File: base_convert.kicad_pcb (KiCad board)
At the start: 2 copper layers, 93.3 x 100 mm, 96 parts, among them J1 ISP, J3 Vin, Q1 Q_PMOS_GSD, Q10 Q_PNP_BEC, Q11 Q_PNP_BEC, Q12 Q_PNP_BEC, Q13 Q_PNP_BEC, Q14 Q_PNP_BEC, Q15 Q_PNP_BEC, Q16 Q_PNP_BEC, Q17 Q_PNP_BEC, Q18 Q_PNP_BEC, Q19 Q_PNP_BEC, Q2 Q_PNP_BEC, Q20 Q_NPN_BEC, Q21 Q_NPN_BEC, Q22 Q_NPN_BEC, Q23 Q_NPN_BEC, Q24 Q_NPN_BEC, Q25 Q_NPN_BEC, Q26 Q_NPN_BEC, Q27 Q_NPN_BEC, Q3 Q_PNP_BEC, Q4 Q_PNP_BEC, Q5 Q_PNP_BEC, Q6 Q_NPN_BEC, Q7 Q_NPN_BEC, Q8 Q_NPN_BEC, Q9 Q_NPN_BEC, SW1 SELECT, SW10 1, SW11 4, SW12 7, SW13 A, SW14 CLEAR, SW15 B, SW16 C, SW17 D, SW18 E, SW2 3, SW3 6, SW4 9, SW5 F, SW6 2, SW7 5, SW8 8, SW9 0, U1 MIC5317-3.3YM5-TR, U2 MSP430FR2033IPMR

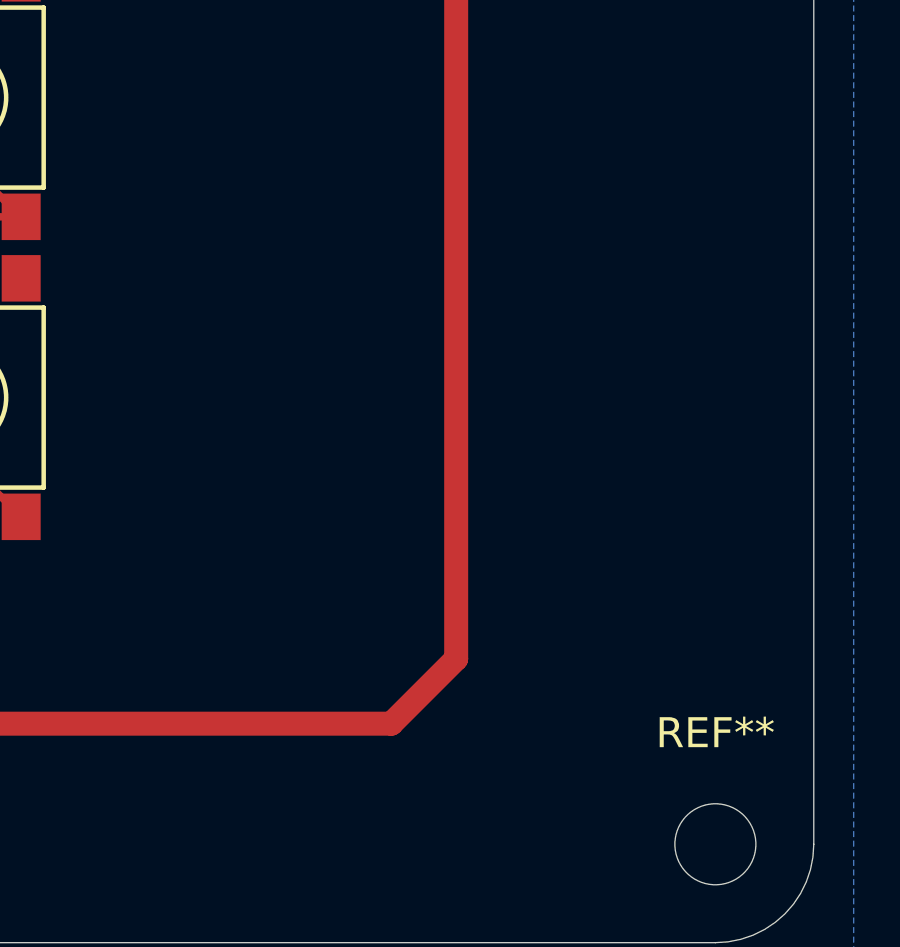
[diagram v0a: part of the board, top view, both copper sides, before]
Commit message: add logo
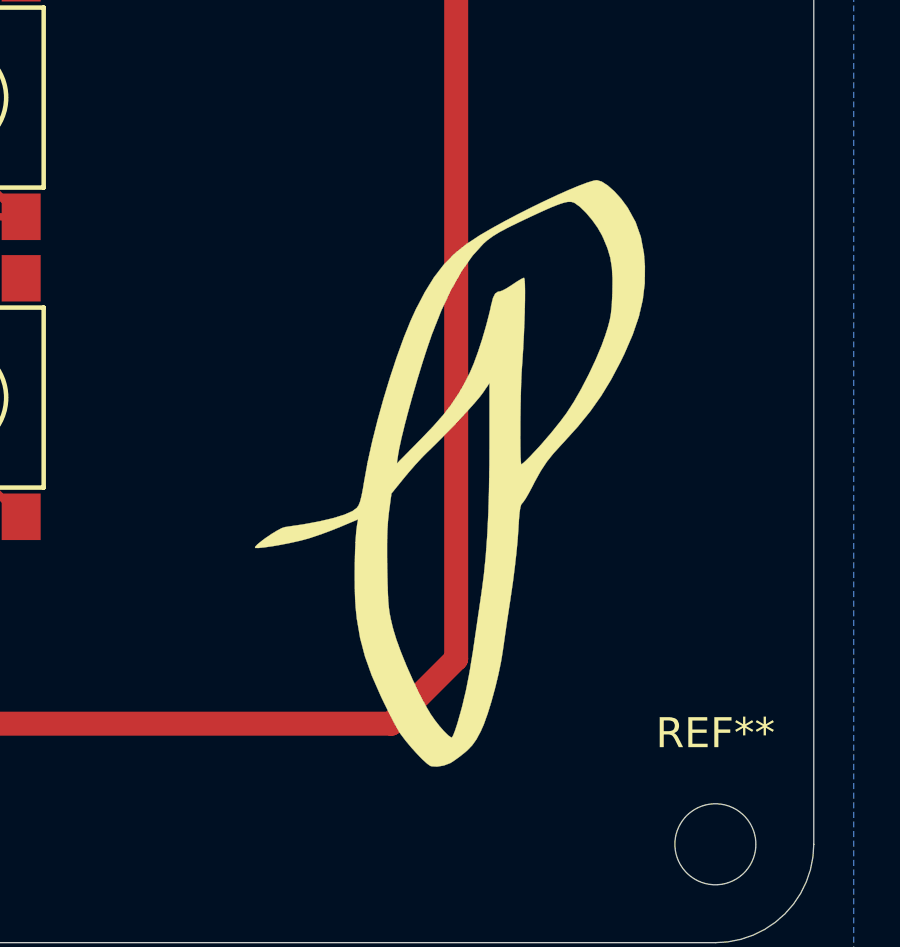
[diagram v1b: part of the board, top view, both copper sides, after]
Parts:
- added G***: LOGO, PL_logo:logo_height_20mm, F.Cu at (134.5, 134.4)
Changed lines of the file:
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@@
 (kicad_pcb (version 4) (host pcbnew 4.0.7)
   (general
-    (links 237)
+    (links 0)
     (no_connects 0)
     (area 52 48.605 148.000001 151.000001)
@@
     (tracks 1310)
     (zones 0)
-    (modules 96)
+    (modules 97)
     (nets 112)
   )
@@
     (34 B.Paste user hide)
     (35 F.Paste user hide)
-    (36 B.SilkS user hide)
-    (37 F.SilkS user hide)
+    (36 B.SilkS user)
+    (37 F.SilkS user)
     (38 B.Mask user hide)
     (39 F.Mask user hide)
@@
     (pad 1 np_thru_hole circle (at 0 0) (size 2.7 2.7) (drill 2.7) (layers *.Cu *.Mask))
   )
+  (module PL_logo:logo_height_20mm (layer F.Cu)
+    (at 134.49 134.4)
+    (fp_text reference G*** (at 0 0) (layer F.SilkS) hide
+      (effects (font (thickness 0.3)))
+    )
+    (fp_text value LOGO (at 0.75 0) (layer F.SilkS) hide
+      (effects (font (thickness 0.3)))
+    )
+    (fp_poly (pts (xy 5.110447 -9.770652) (xy 5.312269 -9.640666) (xy 5.534322 -9.443902) (xy 5.758485 -9.196577)
+      (xy 5.96664 -8.914909) (xy 5.98231 -8.890989) (xy 6.239473 -8.422228) (xy 6.416068 -7.923876)
+      (xy 6.519396 -7.371012) (xy 6.551677 -6.947643) (xy 6.545956 -6.381247) (xy 6.479614 -5.82589)
+      (xy 6.347459 -5.261244) (xy 6.144301 -4.666981) (xy 5.864947 -4.022772) (xy 5.737802 -3.760784)
+      (xy 5.422669 -3.165189) (xy 5.093822 -2.62529) (xy 4.731023 -2.1127) (xy 4.314034 -1.599035)
+      (xy 3.822617 -1.055909) (xy 3.768597 -0.998877) (xy 3.49642 -0.699627) (xy 3.277407 -0.423662)
+      (xy 3.085305 -0.133221) (xy 2.89386 0.209456) (xy 2.796977 0.398632) (xy 2.681419 0.617345)
+      (xy 2.574296 0.800024) (xy 2.491792 0.919921) (xy 2.464519 0.948195) (xy 2.427285 0.998544)
+      (xy 2.397557 1.099049) (xy 2.373053 1.26548) (xy 2.351492 1.513606) (xy 2.330594 1.859196)
+      (xy 2.329359 1.882471) (xy 2.305361 2.215766) (xy 2.265794 2.627183) (xy 2.214545 3.082356)
+      (xy 2.155502 3.54692) (xy 2.09255 3.986509) (xy 2.088075 4.015605) (xy 2.026235 4.419717)
+      (xy 1.966076 4.820335) (xy 1.911374 5.191749) (xy 1.865906 5.508247) (xy 1.833449 5.744119)
+      (xy 1.827804 5.787522) (xy 1.764501 6.187507) (xy 1.67347 6.63336) (xy 1.562106 7.097654)
+      (xy 1.437803 7.552962) (xy 1.307955 7.971858) (xy 1.179956 8.326913) (xy 1.084112 8.546046)
+      (xy 0.937302 8.819355) (xy 0.794637 9.022883) (xy 0.62642 9.195872) (xy 0.530816 9.277194)
+      (xy 0.347846 9.420104) (xy 0.178277 9.542154) (xy 0.059975 9.616254) (xy -0.151123 9.695147)
+      (xy -0.374715 9.732273) (xy -0.561955 9.720841) (xy -0.600957 9.708124) (xy -0.708554 9.634028)
+      (xy -0.865156 9.490665) (xy -1.050824 9.299752) (xy -1.245621 9.08301) (xy -1.429608 8.862157)
+      (xy -1.582846 8.658913) (xy -1.634056 8.582753) (xy -1.724533 8.427502) (xy -1.849762 8.193559)
+      (xy -1.996847 7.905971) (xy -2.152891 7.589783) (xy -2.253941 7.378834) (xy -2.553552 6.696073)
+      (xy -2.780259 6.060909) (xy -2.943151 5.441507) (xy -3.051318 4.806034) (xy -3.089538 4.452134)
+      (xy -3.108839 4.147395) (xy -3.120082 3.777455) (xy -3.123672 3.36871) (xy -3.120014 2.947556)
+      (xy -3.109511 2.540389) (xy -3.097113 2.272005) (xy -2.042954 2.272005) (xy -2.04283 2.749466)
+      (xy -2.036487 3.167865) (xy -2.027131 3.598264) (xy -2.016838 3.936345) (xy -2.003406 4.203938)
+      (xy -1.984633 4.422876) (xy -1.95832 4.61499) (xy -1.922265 4.802112) (xy -1.874267 5.006072)
+      (xy -1.835999 5.156553) (xy -1.730964 5.501704) (xy -1.579822 5.91545) (xy -1.39543 6.368634)
+      (xy -1.190641 6.832099) (xy -0.978312 7.276687) (xy -0.771297 7.673242) (xy -0.592437 7.97709)
+      (xy -0.449521 8.183624) (xy -0.292517 8.38383) (xy -0.138809 8.558643) (xy -0.005783 8.689)
+      (xy 0.089178 8.755836) (xy 0.119772 8.758103) (xy 0.157698 8.692735) (xy 0.21601 8.544905)
+      (xy 0.284254 8.342064) (xy 0.309684 8.259381) (xy 0.460399 7.720907) (xy 0.589537 7.175597)
+      (xy 0.704348 6.589349) (xy 0.81208 5.928063) (xy 0.827759 5.822461) (xy 0.888257 5.410055)
+      (xy 0.957618 4.936465) (xy 1.028263 4.453473) (xy 1.092615 4.012863) (xy 1.107636 3.909887)
+      (xy 1.183113 3.33022) (xy 1.244733 2.715647) (xy 1.2932 2.052558) (xy 1.329222 1.327348)
+      (xy 1.353506 0.526409) (xy 1.366756 -0.363868) (xy 1.369888 -1.142652) (xy 1.369888 -3.052185)
+      (xy 1.159111 -2.739014) (xy 1.043555 -2.587637) (xy 0.860782 -2.372867) (xy 0.625694 -2.110611)
+      (xy 0.35319 -1.816778) (xy 0.058172 -1.507274) (xy -0.244461 -1.198009) (xy -0.539807 -0.90489)
+      (xy -0.732942 -0.719056) (xy -0.897814 -0.551888) (xy -1.103188 -0.327672) (xy -1.31941 -0.079417)
+      (xy -1.467688 0.09879) (xy -1.897581 0.627835) (xy -1.980084 1.241445) (xy -2.01215 1.537418)
+      (xy -2.032917 1.874463) (xy -2.042954 2.272005) (xy -3.097113 2.272005) (xy -3.092567 2.173606)
+      (xy -3.069586 1.873602) (xy -3.047424 1.701141) (xy -3.011222 1.490147) (xy -3.603252 1.740546)
+      (xy -3.913187 1.864764) (xy -4.253148 1.990126) (xy -4.570058 2.097455) (xy -4.708989 2.140026)
+      (xy -4.961993 2.20636) (xy -5.256046 2.2724) (xy -5.565525 2.333672) (xy -5.864807 2.385699)
+      (xy -6.128268 2.424005) (xy -6.330287 2.444114) (xy -6.440733 2.44253) (xy -6.443846 2.406481)
+      (xy -6.369386 2.326813) (xy -6.238015 2.218057) (xy -6.070397 2.094748) (xy -5.887193 1.971418)
+      (xy -5.709067 1.862599) (xy -5.55668 1.782823) (xy -5.45142 1.746718) (xy -4.82984 1.654577)
+      (xy -4.286919 1.553549) (xy -3.829866 1.445555) (xy -3.465892 1.332515) (xy -3.202205 1.21635)
+      (xy -3.053996 1.107951) (xy -2.995972 1.025898) (xy -2.945791 0.904301) (xy -2.898135 0.723744)
+      (xy -2.847687 0.464808) (xy -2.801264 0.185151) (xy -2.699695 -0.371012) (xy -1.71808 -0.371012)
+      (xy -0.912748 -1.18778) (xy -0.506321 -1.612275) (xy -0.173333 -1.990833) (xy 0.103453 -2.346866)
+      (xy 0.341276 -2.703785) (xy 0.557374 -3.085004) (xy 0.713275 -3.39618) (xy 0.845662 -3.705274)
+      (xy 0.988099 -4.093966) (xy 1.130249 -4.529533) (xy 1.261771 -4.97925) (xy 1.372328 -5.410396)
+      (xy 1.424366 -5.646894) (xy 1.486632 -5.890114) (xy 1.559501 -6.035739) (xy 1.653241 -6.10033)
+      (xy 1.709886 -6.107416) (xy 1.803792 -6.138716) (xy 1.956032 -6.220771) (xy 2.133521 -6.335731)
+      (xy 2.304954 -6.449923) (xy 2.443933 -6.5318) (xy 2.520975 -6.564026) (xy 2.521823 -6.564045)
+      (xy 2.539593 -6.509571) (xy 2.550554 -6.356119) (xy 2.555057 -6.118642) (xy 2.553451 -5.812094)
+      (xy 2.546088 -5.45143) (xy 2.533316 -5.051604) (xy 2.515486 -4.627569) (xy 2.492949 -4.19428)
+      (xy 2.466053 -3.766691) (xy 2.451665 -3.567416) (xy 2.437554 -3.331244) (xy 2.425449 -3.03294)
+      (xy 2.41546 -2.689467) (xy 2.4077 -2.317787) (xy 2.402282 -1.934861) (xy 2.399317 -1.557652)
+      (xy 2.398917 -1.20312) (xy 2.401195 -0.888229) (xy 2.406263 -0.629939) (xy 2.414232 -0.445213)
+      (xy 2.425215 -0.351011) (xy 2.430349 -0.342472) (xy 2.484805 -0.38002) (xy 2.592384 -0.477421)
+      (xy 2.701472 -0.585057) (xy 3.055369 -0.96369) (xy 3.416394 -1.381698) (xy 3.749052 -1.796963)
+      (xy 3.938592 -2.05297) (xy 4.174713 -2.416169) (xy 4.426061 -2.855489) (xy 4.675934 -3.337451)
+      (xy 4.907627 -3.828575) (xy 5.104436 -4.295382) (xy 5.228975 -4.63929) (xy 5.316414 -4.916881)
+      (xy 5.37705 -5.143794) (xy 5.416914 -5.356555) (xy 5.442038 -5.591687) (xy 5.458451 -5.885713)
+      (xy 5.465453 -6.071296) (xy 5.471388 -6.527629) (xy 5.450072 -6.904527) (xy 5.395514 -7.234718)
+      (xy 5.301721 -7.550929) (xy 5.162699 -7.885885) (xy 5.114386 -7.988458) (xy 4.972109 -8.238033)
+      (xy 4.788131 -8.495248) (xy 4.584747 -8.734412) (xy 4.384252 -8.929835) (xy 4.208941 -9.055824)
+      (xy 4.173444 -9.07273) (xy 4.09124 -9.094614) (xy 3.989089 -9.094277) (xy 3.855089 -9.067416)
+      (xy 3.677339 -9.00973) (xy 3.443938 -8.91692) (xy 3.142982 -8.784682) (xy 2.762572 -8.608718)
+      (xy 2.356567 -8.416162) (xy 1.985432 -8.234109) (xy 1.699223 -8.081259) (xy 1.476723 -7.944798)
+      (xy 1.296718 -7.811912) (xy 1.167101 -7.697722) (xy 0.803408 -7.29618) (xy 0.446701 -6.788609)
+      (xy 0.101554 -6.183108) (xy -0.227457 -5.487781) (xy -0.535755 -4.71073) (xy -0.563786 -4.632993)
+      (xy -0.715261 -4.192448) (xy -0.873007 -3.703403) (xy -1.031467 -3.185769) (xy -1.185084 -2.659456)
+      (xy -1.328301 -2.144377) (xy -1.455563 -1.66044) (xy -1.561311 -1.227556) (xy -1.639989 -0.865638)
+      (xy -1.681547 -0.627866) (xy -1.71808 -0.371012) (xy -2.699695 -0.371012) (xy -2.689515 -0.426754)
+      (xy -2.541231 -1.098048) (xy -2.363085 -1.806575) (xy -2.161753 -2.53018) (xy -1.943909 -3.246706)
+      (xy -1.716226 -3.933999) (xy -1.485378 -4.569901) (xy -1.258041 -5.132258) (xy -1.086226 -5.50809)
+      (xy -0.781415 -6.091052) (xy -0.478181 -6.580316) (xy -0.160039 -6.994905) (xy 0.189496 -7.35384)
+      (xy 0.58691 -7.676144) (xy 1.048687 -7.980837) (xy 1.065546 -7.991012) (xy 1.442899 -8.210713)
+      (xy 1.858246 -8.439635) (xy 2.297431 -8.671115) (xy 2.746294 -8.89849) (xy 3.19068 -9.115098)
+      (xy 3.61643 -9.314276) (xy 4.009387 -9.489361) (xy 4.355394 -9.633692) (xy 4.640293 -9.740605)
+      (xy 4.849927 -9.803437) (xy 4.946973 -9.817643) (xy 5.110447 -9.770652)) (layer F.SilkS) (width 0.01))
+  )
   (gr_line (start 141.67 55) (end 58.33 55) (layer Dwgs.User) (width 0.01))

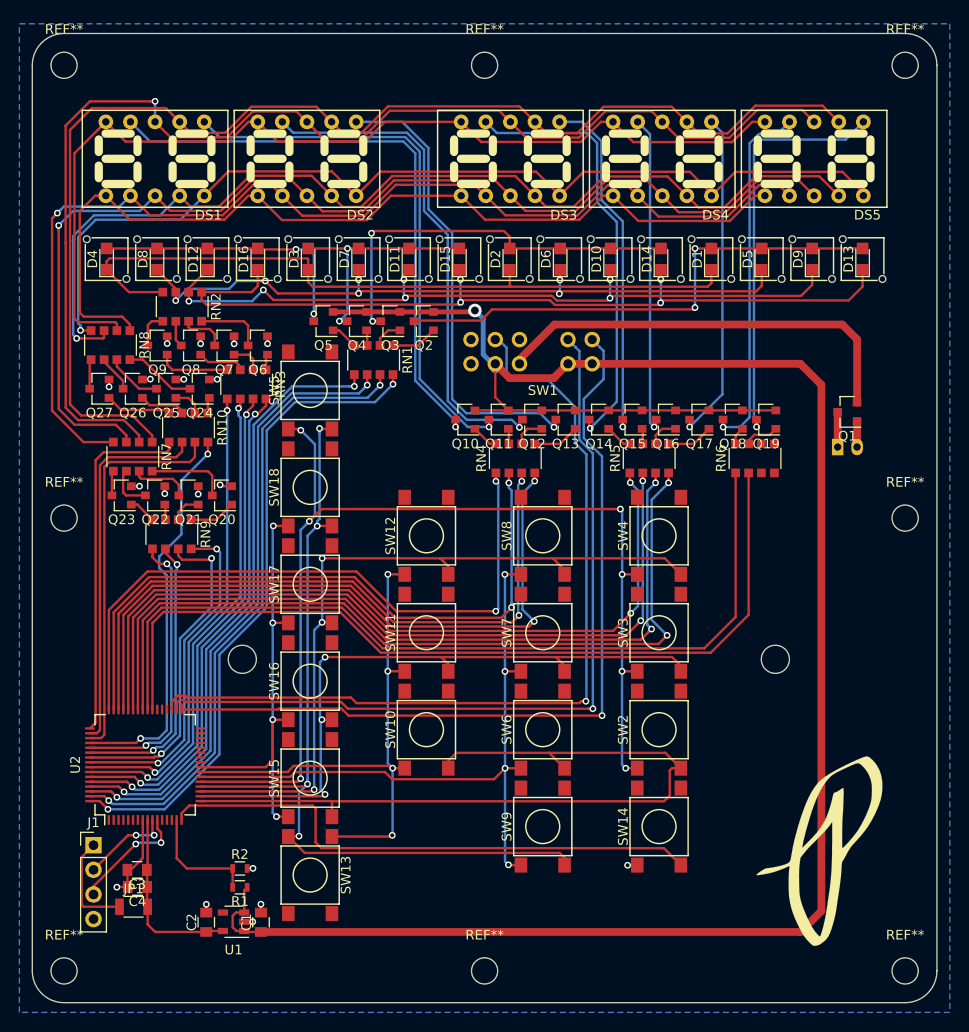
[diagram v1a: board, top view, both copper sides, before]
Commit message: clean up silkscreen, as sn label
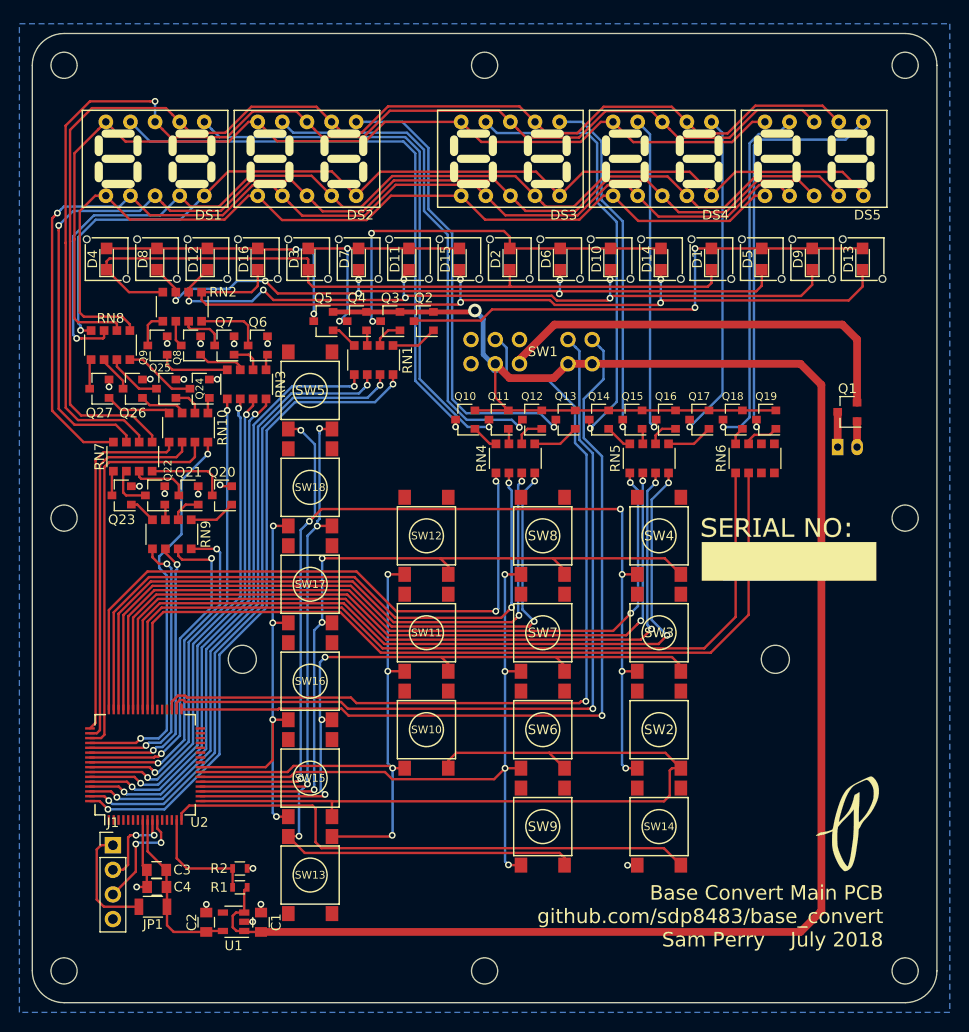
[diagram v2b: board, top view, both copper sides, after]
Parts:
- added G***: LOGO, Artwork:sn_label, F.Cu at (131.4, 103.2)
- G***: footprint PL_logo:logo_height_20mm -> PL_logo:logo_height_10mm
- moved G*** 4.07 mm to (137.4, 131.6)
- moved C3 2.00 mm to (66.2, 136.3)
- moved C4 2.00 mm to (66.2, 138.1)
- moved J1 2.00 mm to (61.6, 133.8)
- moved JP1 2.00 mm to (65.8, 140.1)
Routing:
- net +3V3: track 19.0 -> 17.9 mm
- net Net-(J1-Pad1): track 10.7 -> 11.7 mm
- net /SBWTCK: track 12.2 -> 11.3 mm
- net GND: track 25.8 -> 25.1 mm
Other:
- board text added: "Base Convert Main PCB github.com/sdp8483/base_convert Sam Perry July 2018"
